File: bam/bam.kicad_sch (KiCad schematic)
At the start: 25 parts, among them J1 battery, Q1 VP3203N3-G, Q2 PN2222A, Q3 PN2222A, SW1 on/off, SW2 next, SW3 previous, U1 NE555P

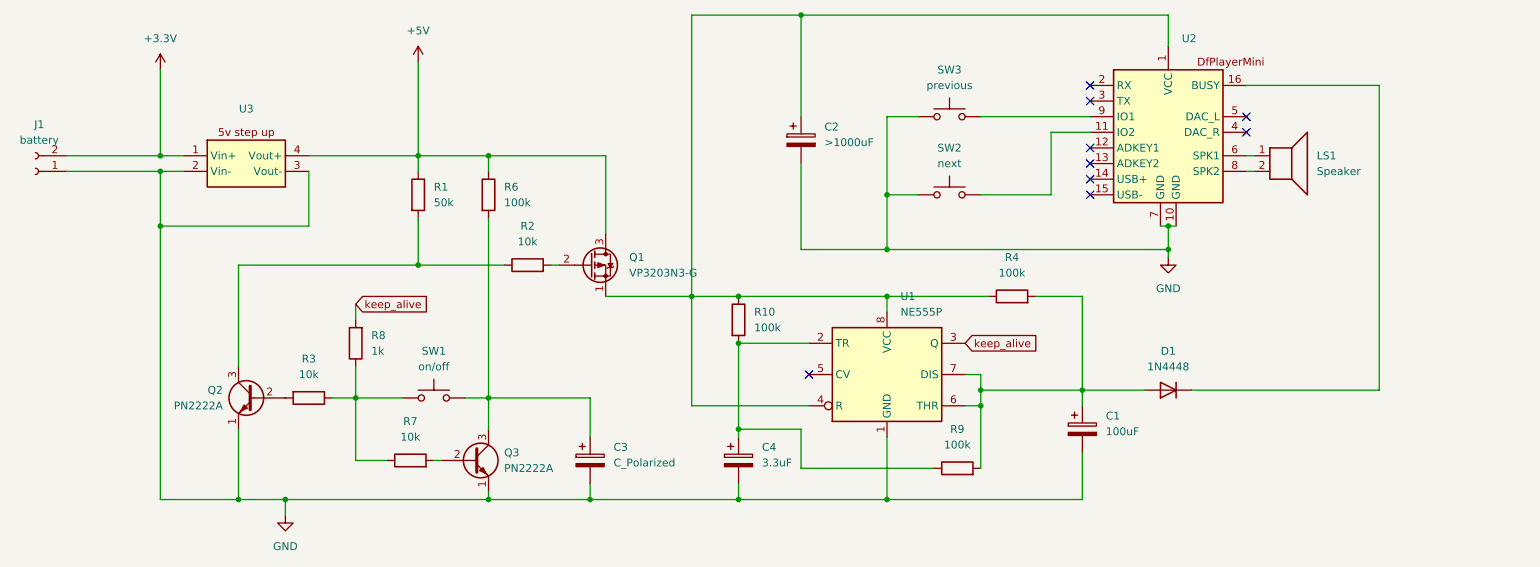
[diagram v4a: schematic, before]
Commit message: battery life improvements
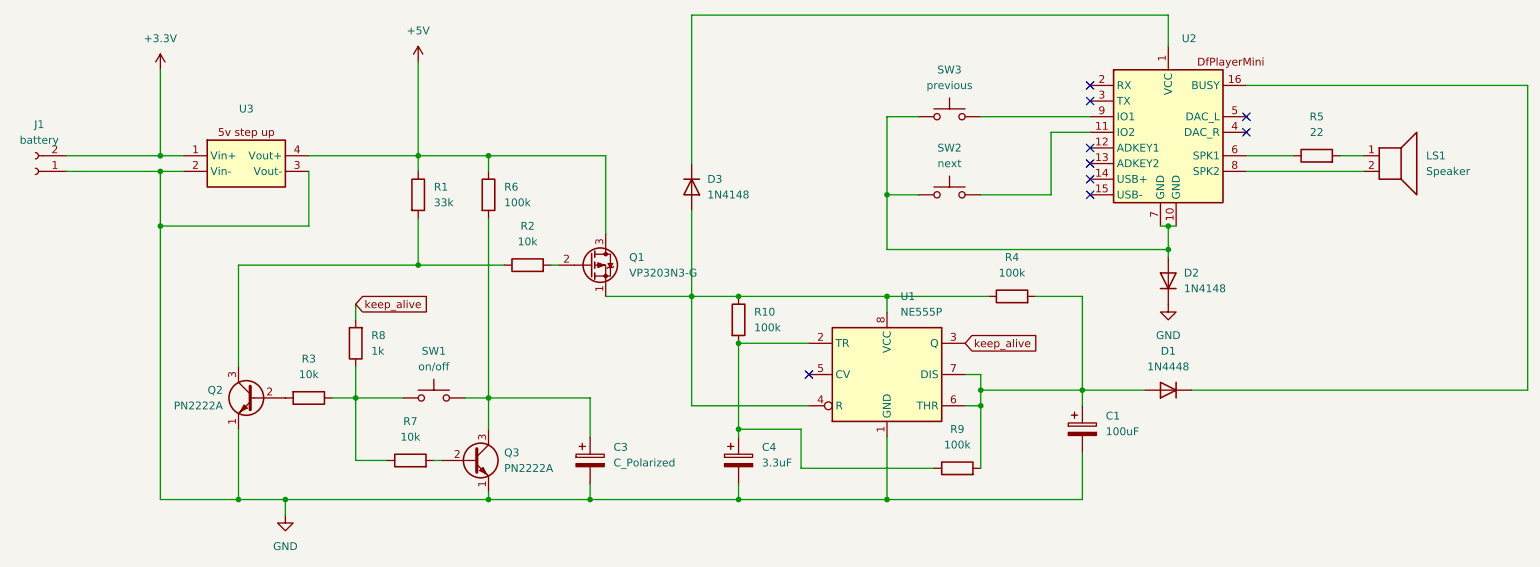
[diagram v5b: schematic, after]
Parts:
- removed C2: >1000uF, symbol Device:C_Polarized
- added D2, D3: 1N4148, Diode_THT:D_DO-35_SOD27_P7.62mm_Horizontal, symbol Diode:1N4148
- added R5: 22, symbol Device:R
- R1: value 50k -> 33k
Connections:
- net GND: now also D2.1 (K); no longer SW2.1, SW3.1, U2.10 (GND), U2.7 (GND)
- net at Q1.1 (S), R10.1, R4.1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: now also D3.2 (A); no longer U2.1 (VCC)
- net at LS1.1: now also R5.2; no longer U2.6 (SPK1)
- new net: D3.1 (K), U2.1 (VCC)
- new net: D2.2 (A), SW2.1, SW3.1, U2.10 (GND), U2.7 (GND)
- new net: R5.1, U2.6 (SPK1)
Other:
- moved on the sheet: LS1

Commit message: minor updates
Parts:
- removed R5: 22, symbol Device:R
- added C2: C, symbol Device:C
- added R11: 10, symbol Device:R
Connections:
- net GND: now also C2.1
- net at LS1.1: now also U2.6 (SPK1)
- net at LS1.2: now also R11.2; no longer U2.8 (SPK2)
- net at D2.2 (A), SW2.1, SW3.1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: now also R11.1
- net at U1.5 (CV): now also C2.2
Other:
- moved on the sheet: C4, J1, LS1, R10
